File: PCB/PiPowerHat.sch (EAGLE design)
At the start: 30 parts, among them IC1 7805T, K1 PIN20X2, U1 EEPROM24, U2 INA219AIDCNRSOIC, U4 DS18B20, U5 DS1820SOIC

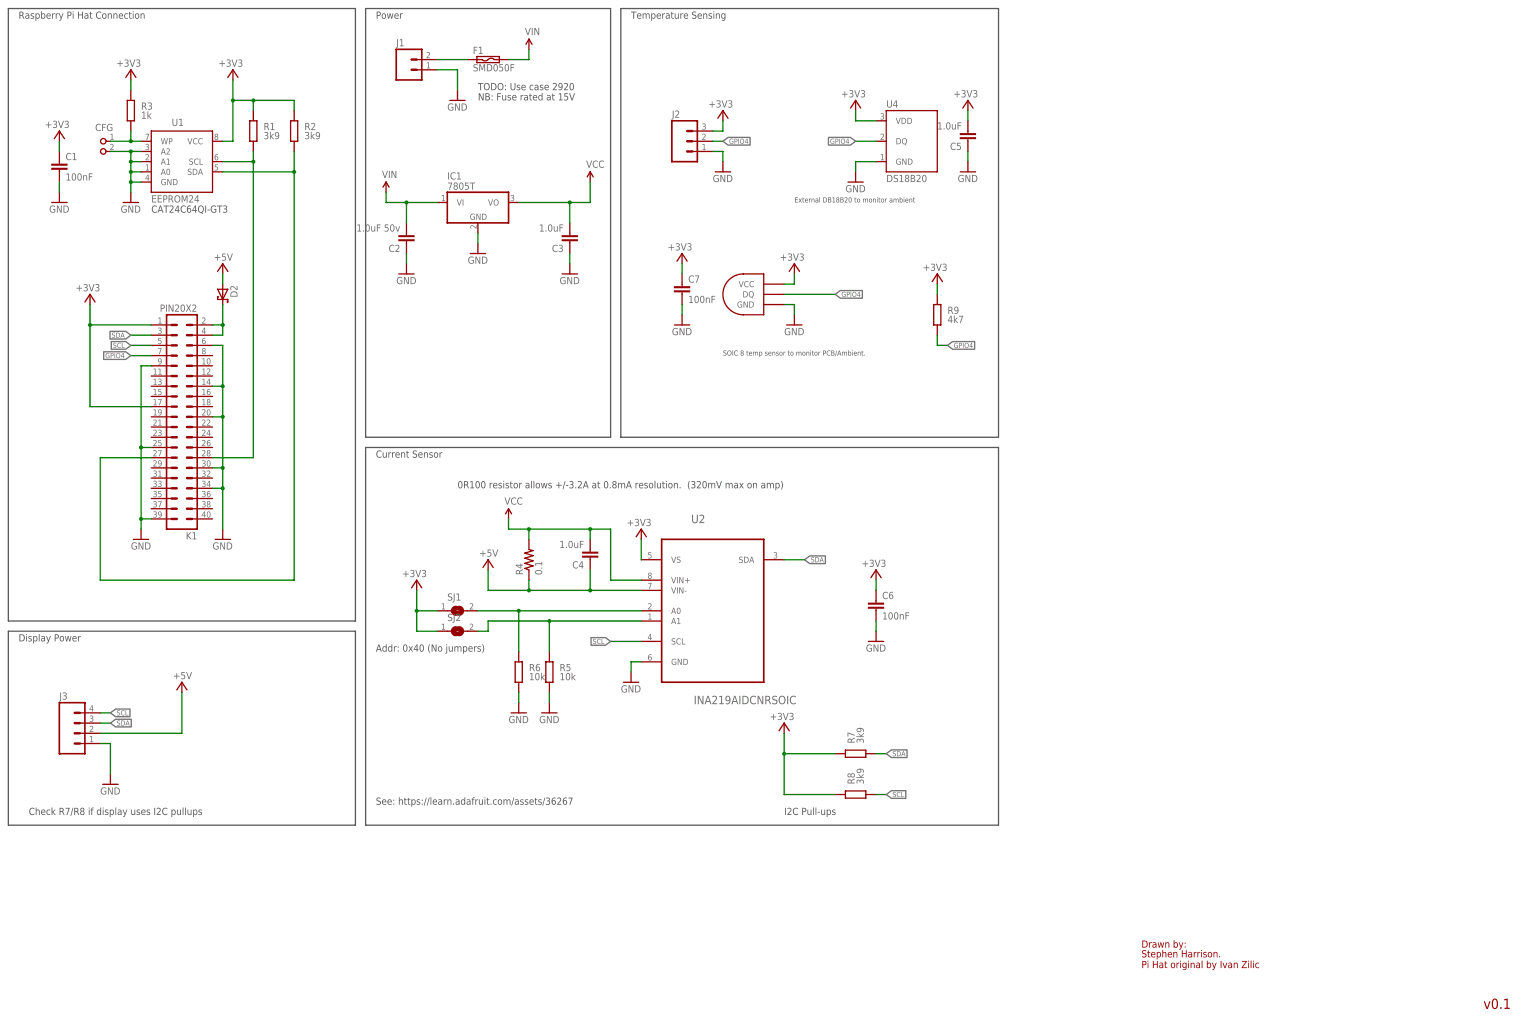
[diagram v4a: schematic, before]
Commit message: Improved routing to increase ground plain, change IO pins used with option to select between 2 IO pins for temperature sensors.
Added OSH logo and rear LED.
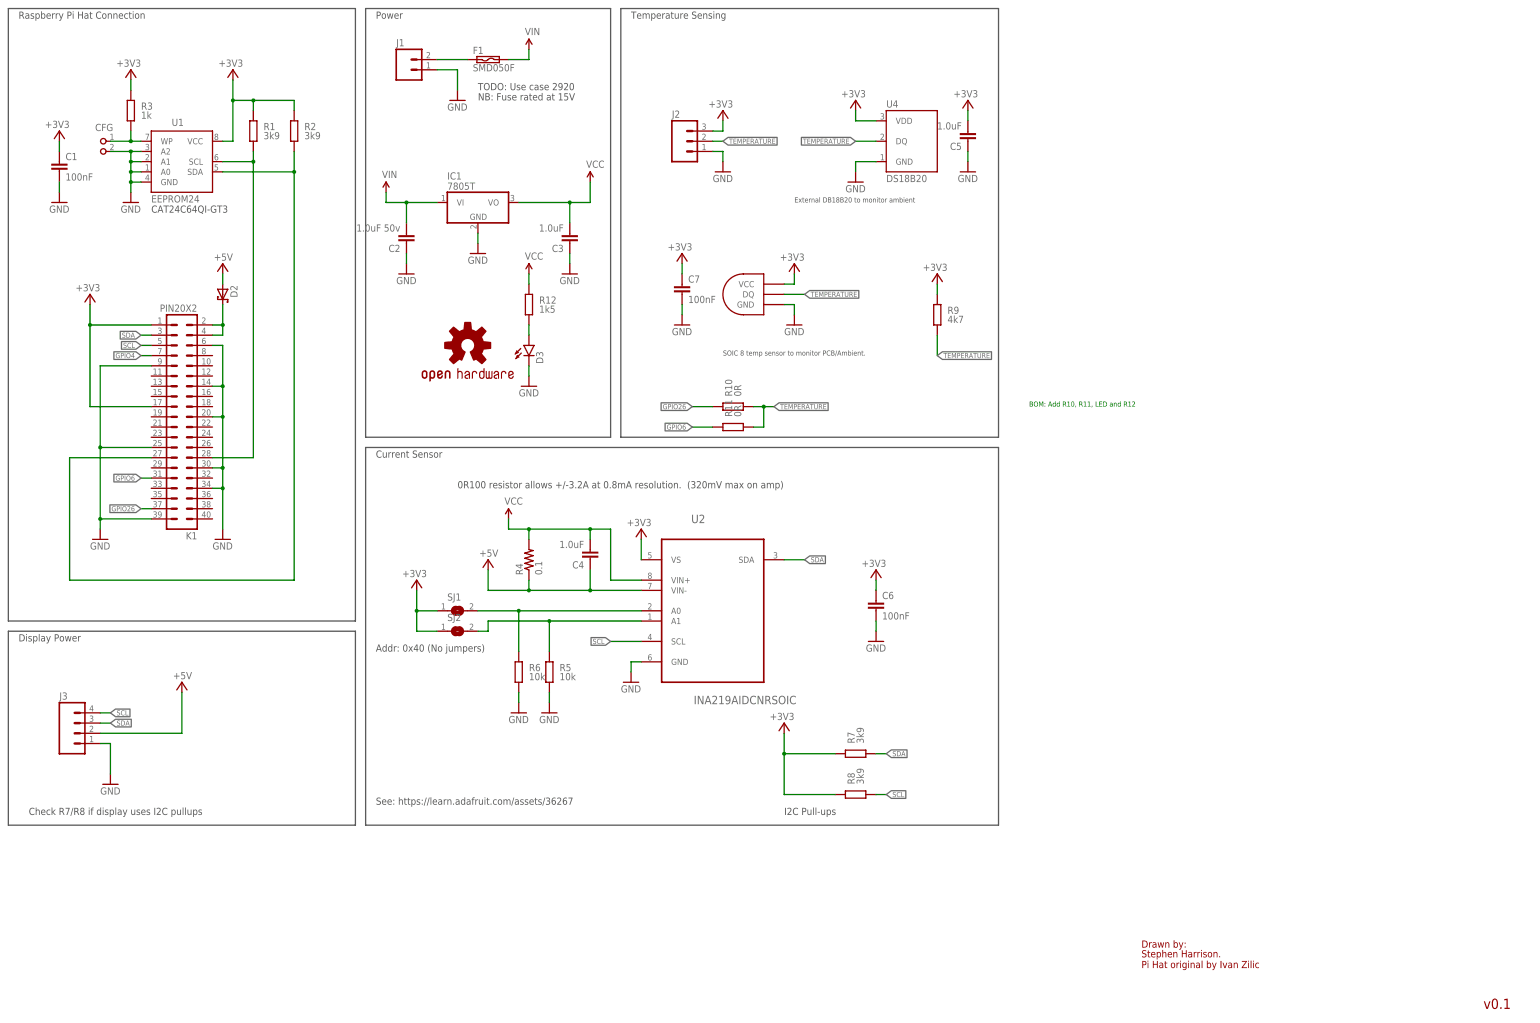
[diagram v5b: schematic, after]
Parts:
- added D3: (no value), SparkFun-LED:LED1206-BOTTOM
- added LOGO1: OSHW-LOGOM, SparkFun-Aesthetics:OSHW-LOGOM
- added R10, R11: 0R, resistor:R-EU_M0805
- added R12: 1k5, resistor:R-EU_M0805
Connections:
- new net GPIO26: K1.37, R10.2
- new net GPIO6: K1.31, R11.2
- new net N$4: D3.A, R12.1
- new net TEMPERATURE: J2.2, R10.1, R11.1, R9.1, U4.DQ, U5.DQ
- net GND: now also D3.C
- net GPIO4: no longer J2.2, R9.1, U4.DQ, U5.DQ
- net VCC: now also R12.2
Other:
- note added: "BOM: Add R10, R11, LED and R12"

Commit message: Changed 7805 style regulator to the 3A buck regulator.
Added DotStar LED strip connector (clk/data).

Added 2 GPIO port + power connector.

Added 2x fan connectors (1x 4 pin PWM, 1x 3 pin PWM power)

Added fuse.

Moved current/voltage sensor to pre-regulator to monitor the input voltage.

Moved board temperature sensor to be under regulator module.
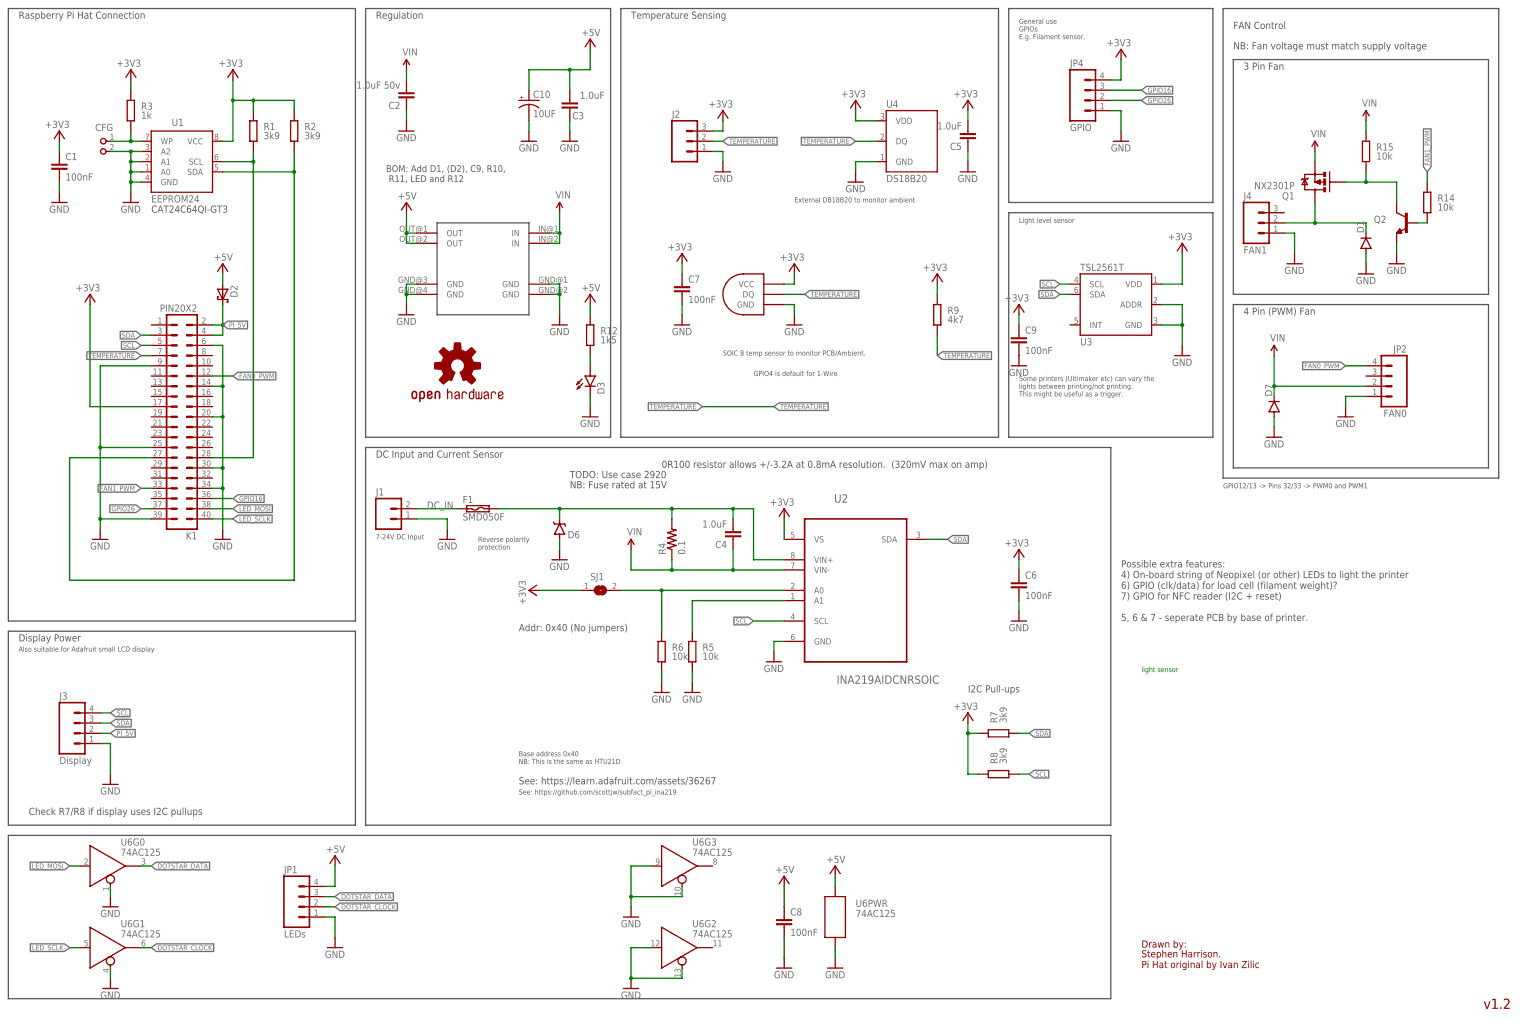
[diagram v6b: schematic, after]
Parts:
- removed IC1: 7805T, linear:7805T
- removed R10, R11: 0R, resistor:R-EU_M0805
- removed SJ2: (no value), jumper:SJ
- added C10: 10UF, SparkFun-Capacitors:10UF-25V-10%(SMT-TANT)
- added C8, C9: 100nF, resistor:C-EUC0805K
- added D1, D7: (no value), SparkFun-DiscreteSemi:DIODESOD123
- added D6: B340A, SparkFun-DiscreteSemi:DIODE-SCHOTTKY-B340A
- added J4: FAN1, SparkFun-Connectors:M03POLAR
- added JP1: LEDs, SparkFun-Connectors:M04POLAR
- added JP2: FAN0, SparkFun-Connectors:M04POLAR
- added JP4: GPIO, SparkFun-Connectors:M04POLAR
- added Q1: NX2301P, SparkFun-DiscreteSemi:MOSFET-PCHANNEL
- added Q2: (no value), SparkFun-DiscreteSemi:TRANSISTOR_NPNSOT23-3
- added R14, R15: 10k, resistor:R-EU_M0805
- added U$1: MINI-BUCK-MODULE-3A, Tinamous:MINI-BUCK-MODULE-3A
- added U3: TSL2561T, SparkFun-Sensors:TSL2561T
- added U6: 74AC125, SparkFun-DigitalIC:74AC125DG125
- D2: value (none) -> MBRS340T3G; FARNELL (none) -> 9557377
- J3: value (none) -> Display
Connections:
- net N$1 renamed DC_IN
- removed net GPIO4: K1.7
- removed net GPIO6: K1.31, R11.2
- removed net N$2: D2.C, K1.2, K1.4
- removed net VCC: C3.2, C4.2, IC1.VO, R12.2, R4.2, U2.VIN+
- new net DOTSTAR_CLOCK: JP1.2, U6G1.Q
- new net DOTSTAR_DATA: JP1.3, U6G0.Q
- new net FAN0_PWM: JP2.4, K1.12
- new net FAN1_PWM: K1.33, R14.2
- new net GPIO16: JP4.3, K1.36
- new net LED_MOSI: K1.38, U6G0.D
- new net LED_SCLK: K1.40, U6G1.D
- new net N$13: Q2.B, R14.1
- new net N$5: C4.2, D6.C, F1.2, R4.2, U2.VIN+
- new net N$7: D1.C, J4.2, Q1.D
- new net N$8: Q1.G, Q2.C, R15.1
- new net PI_5V: D2.C, J3.2, K1.2, K1.4
- net +3V3: now also C9.1, JP4.4, U3.VDD; no longer K1.1, SJ2.1
- net +5V: now also C10.+, C3.2, C8.1, JP1.4, R12.2, U$1.OUT@1, U$1.OUT@2, U6PWR.P$V+; no longer C4.1, J3.2, R4.1, U2.VIN-
- net GND: now also C10.-, C8.2, C9.2, D1.A, D6.A, D7.A, J4.1, JP1.1, JP2.1, JP4.1, Q2.E, U$1.GND@1, U$1.GND@2, U$1.GND@3, U$1.GND@4, U3.ADDR, U3.GND, U6G0.!EN, U6G1.!EN, U6G2.!EN, U6G2.D, U6G3.!EN, U6G3.D, U6PWR.P$V-; no longer IC1.GND
- net GPIO26: now also JP4.2; no longer R10.2
- net N$10: no longer SJ2.2
- net SCL: now also U3.SCL
- net SDA: now also U3.SDA
- net TEMPERATURE: now also K1.7; no longer R10.1, R11.1
- net VIN: now also C4.1, D7.C, JP2.2, Q1.S, R15.2, R4.1, U$1.IN@1, U$1.IN@2, U2.VIN-; no longer F1.2, IC1.VI
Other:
- note added: "3 Pin Fan"
- note added: "4 Pin (PWM) Fan"
- note added: "7-24V DC Input"
- note added: "Also suitable for Adafruit small LCD display"
- note added: "BOM: Add D1, (D2), C9, R10, R11, LED and R12"
- note added: "Base address 0x40 NB: This is the same as HTU21D"
- note added: "DC Input and Current Sensor"
- note added: "FAN Control"
- note added: "GPIO12/13 -> Pins 32/33 -> PWM0 and PWM1"
- note added: "GPIO4 is default for 1-Wire"
- note added: "General use GPIOs E.g. Filament sensor."
- note added: "Light level sensor"
- note added: "NB: Fan voltage must match supply voltage"
- note added: "Possible extra features: 4) On-board string of Neopixel (or other) LEDs to light the printer 6) GPIO (clk/data) for load cell (filament weight)? 7) GPIO for NFC reader (I2C + reset) 5, 6 & 7 - seperate PCB by base of printer."
- note added: "Regulation"
- note added: "Reverse polarity protection"
- note added: "See: https://github.com/scottjw/subfact_pi_ina219"
- note added: "Some printers (Ultimaker etc) can vary the lights between printing/not printing. This might be useful as a trigger."
- note added: "light sensor"
- note added: "v1.2"
- note removed: "BOM: Add R10, R11, LED and R12"
- note removed: "Current Sensor"
- note removed: "Power"
- note removed: "v0.1"
- moved on the sheet: C2, C3, C4, C6, D3, F1, J1, R12, R4, R5, R6, R7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

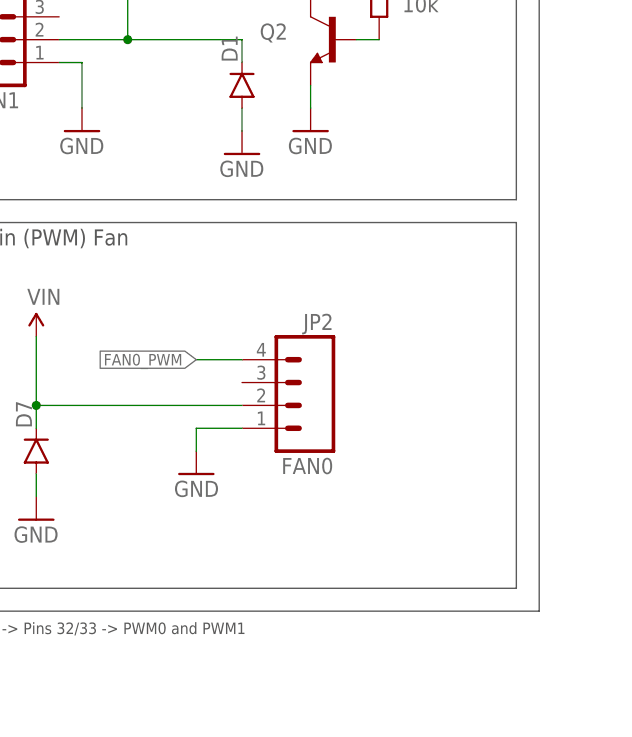
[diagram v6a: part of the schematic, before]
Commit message: Added pin numbers for the fans
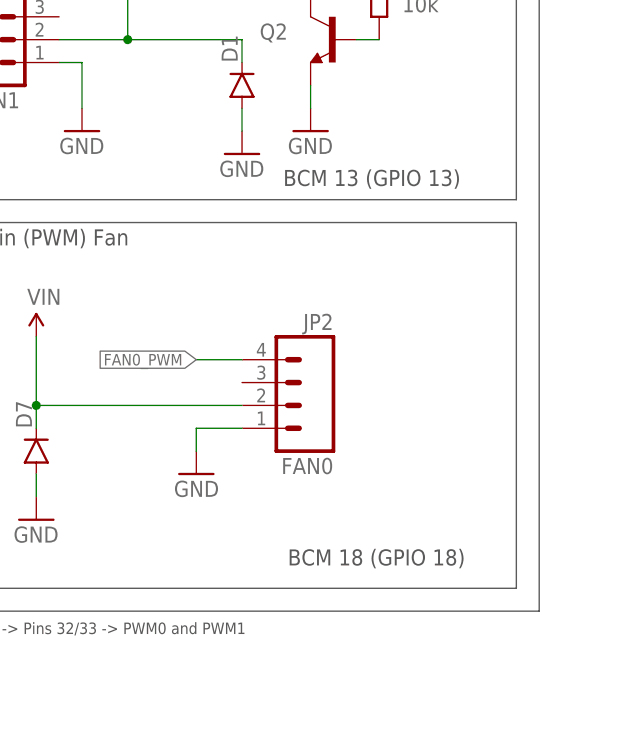
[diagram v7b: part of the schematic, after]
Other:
- note added: "BCM 13 (GPIO 13)"
- note added: "BCM 18 (GPIO 18)"
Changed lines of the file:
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@@
 lights between printing/not printing.
 This might be useful as a trigger.</text>
+<text x="350.52" y="142.24" size="1.778" layer="97">BCM 18 (GPIO 18)</text>
+<text x="350.012" y="184.404" size="1.778" layer="97">BCM 13 (GPIO 13)</text>
 </plain>
 <instances>
